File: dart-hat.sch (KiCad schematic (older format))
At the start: 33 parts, among them J0 XT60 Female, J1 Raspberry_Pi_2_3, Q1 Q_PMOS_DSG, Q2 Q_PMOS_DSG, Q3 DMMT5401, U1 CAT24C32YI-GT3

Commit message: power supply overhaul
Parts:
- C1: renamed from C2; footprint Capacitor_SMD:C_0805_2012Metric_Pad1.15x1.40mm_HandSolder -> Capacitor_SMD:C_0603_1608Metric_Pad1.05x0.95mm_HandSolder; Description (none) -> 25V MLCC 10%; Manufacturer_Part_Number (none) -> GRM188R61E106KA73J; PURCHASE-URL (none) -> https://www.mouser.com/ProductDetail/Murata-Electronics/GRM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; category (none) -> EEPROM; package (none) -> 0603
- C2: renamed from C3; footprint Capacitor_SMD:C_0805_2012Metric_Pad1.15x1.40mm_HandSolder -> Capacitor_SMD:C_0603_1608Metric_Pad1.05x0.95mm_HandSolder; Description (none) -> 16V MLCC 10%; Manufacturer_Part_Number (none) -> C0603C104K4RACTU; category (none) -> EEPROM; package (none) -> 0603
- CP1: Description (none) -> 100V Electrolytic 20%; Manufacturer_Part_Number (none) -> 337CKS050M; category (none) -> LIPO; package (none) -> 16mm
- D1: renamed from D2; footprint Diode_SMD:D_SOD-523 -> Diode_SMD:D_SOT-23_ANK; Description (none) -> 15V Zener Diode 5mA 250mW; Manufacturer_Part_Number (none) -> BZX84C15VLYFHT116; category (none) -> LIPO; package (none) -> SOT-23
- D2: renamed from D8; Description (none) -> 1.2V GREEN LED 20mA; Manufacturer_Part_Number (none) -> HSME-C170; category (none) -> GPIO; package (none) -> 0805
- D3: renamed from D9; Description (none) -> 2.1V Amber LED 20mA; Manufacturer_Part_Number (none) -> HSMA-C170; category (none) -> GPIO; package (none) -> 0805
- D4: renamed from D1; footprint Package_TO_SOT_THT:TO-220-2_Horizontal_TabUp -> Diode_SMD:D_SOD-128; Description (none) -> Schottky Diode; Manufacturer_Part_Number (none) -> RB088LAM-40TR; category (none) -> LIPO; package (none) -> SOD-128-2
- F1: footprint Fuse:Fuse_0805_2012Metric_Pad1.15x1.40mm_HandSolder -> Fuse:Fuse_Bourns_MF-SM_7.98x5.44mm; Description (none) -> 6V Fuse 3A Hold 5A Trip; Manufacturer_Part_Number (none) -> MF-LSMF300X-2; category (none) -> SERVO; package (none) -> 3121/MF-SM_7.98x5.44
- J1: renamed from J0; Description (none) -> Female XT60 Receptacle; Manufacturer_Part_Number (none) -> XT60; category (none) -> LIPO; package (none) -> XT60
- J2: renamed from J1; Description (none) -> Raspberry Pi Stackable Header; category (none) -> PI; package (none) -> 2x20x2.54mm
- JP1: Description (none) -> Pin Header; category (none) -> EEPROM; package (none) -> 2x2.54mm
- Q1: footprint Package_TO_SOT_SMD:TO-263-3_TabPin2 -> Package_TO_SOT_SMD:TO-263-2; Description (none) -> 60V 27.5A P-Channel MOSFET (120W Dissipation); Manufacturer_Part_Number (none) -> NTB25P06T4G; category (none) -> LIPO
- Q2: footprint Package_SO:SOIC-8-1EP_3.9x4.9mm_P1.27mm_EP2.29x3mm -> Package_TO_SOT_SMD:TO-263-2; Description (none) -> 60V 27.5A P-Channel MOSFET (120W Dissipation); Manufacturer_Part_Number (none) -> NTB25P06T4G; category (none) -> 5VREG
- Q3: Manufacturer_Part_Number (none) -> DMMT5401; category (none) -> 5VREG
- R1: footprint Resistor_SMD:R_0805_2012Metric_Pad1.15x1.40mm_HandSolder -> Resistor_SMD:R_0603_1608Metric_Pad1.05x0.95mm_HandSolder; Description (none) -> 375mW Resistor 0.1%; Manufacturer_Part_Number (none) -> PHP00603E1002BST1; category (none) -> LIPO; package (none) -> 0603
- R10: renamed from R8; footprint Resistor_SMD:R_0805_2012Metric_Pad1.15x1.40mm_HandSolder -> Resistor_SMD:R_0402_1005Metric; Description (none) -> 63mW Resistor 0.05%; Manufacturer_Part_Number (none) -> ERA-2VRW1001X; category (none) -> EEPROM; package (none) -> 0402
- R11: renamed from R9; Description (none) -> 125mW Resistor 0.1%; Manufacturer_Part_Number (none) -> ERA-6VEB4701V; category (none) -> CAN; package (none) -> 0805
- R12: renamed from R10; Description (none) -> 125mW Resistor 0.1%; Manufacturer_Part_Number (none) -> ERA-6VEB4701V; category (none) -> CAN; package (none) -> 0805
- R13: renamed from R11; Description (none) -> 125mW Resistor 0.1%; Manufacturer_Part_Number (none) -> ERA-6VEB4701V; category (none) -> CAN; package (none) -> 0805
- R2, R3: footprint Resistor_SMD:R_0805_2012Metric_Pad1.15x1.40mm_HandSolder -> Resistor_SMD:R_0603_1608Metric_Pad1.05x0.95mm_HandSolder; Description (none) -> 375mW Resistor 0.1%; Manufacturer_Part_Number (none) -> PHP00603E1002BST1; category (none) -> 5VREG; package (none) -> 0603
- R4: renamed from R23; Description (none) -> 100V 125mW Resistor 0.1%; Manufacturer_Part_Number (none) -> ERA-6VEB1200V; category (none) -> GPIO; package (none) -> 0805
- R5: renamed from R24; value 120 -> 62; footprint Resistor_SMD:R_0805_2012Metric_Pad1.15x1.40mm_HandSolder -> Resistor_SMD:R_1206_3216Metric_Pad1.42x1.75mm_HandSolder; Description (none) -> 100V 250mW Resistor 0.1%; Manufacturer_Part_Number (none) -> ERA-8AED620V; category (none) -> GPIO; package (none) -> 0805
- R6: renamed from R4; footprint Resistor_SMD:R_0805_2012Metric_Pad1.15x1.40mm_HandSolder -> Resistor_SMD:R_0603_1608Metric_Pad1.05x0.95mm_HandSolder; Description (none) -> 100mW Resistor 0.1%; Manufacturer_Part_Number (none) -> ERA-3VEB3901V; category (none) -> EEPROM; package (none) -> 0603
- R7: renamed from R5; footprint Resistor_SMD:R_0805_2012Metric_Pad1.15x1.40mm_HandSolder -> Resistor_SMD:R_0603_1608Metric_Pad1.05x0.95mm_HandSolder; Description (none) -> 100mW Resistor 0.1%; Manufacturer_Part_Number (none) -> ERA-3VEB3901V; category (none) -> EEPROM; package (none) -> 0603
- R8: renamed from R6; Description (none) -> 125mW Resistor 0.1%; Manufacturer_Part_Number (none) -> ERA-6VEB4701V; category (none) -> PI; package (none) -> 0805
- R9: renamed from R7; Description (none) -> 125mW Resistor 0.1%; Manufacturer_Part_Number (none) -> ERA-6VEB4701V; category (none) -> PI; package (none) -> 0805
- U1: Description (none) -> 32kb EEPROM i2c 1mhz; Manufacturer_Part_Number (none) -> CAT24C32YI-GT3; category (none) -> EEPROM; package (none) -> 8-TSSOP
- renumbered TP15 to TP1, TP1 to TP2, TP2 to TP3, TP3 to TP4, TP4 to TP5
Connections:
- net +5V: now also F1.1, TP4.1
- net +5V_SRV: no longer F1.1, TP4.1
- net BEC (pi)/V_OUT renamed 5V Power Supply/VOUT

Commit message: final final sch
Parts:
- removed Q1, Q2: Q_PMOS_DSG, Package_TO_SOT_SMD:TO-263-2, symbol Device:Q_PMOS_DSG
- removed TP3: TestPoint, TestPoint:TestPoint_Pad_D1.0mm, symbol Connector:TestPoint
- added Q1, Q2: SI7611DN-T1-GE3, SI7611DN-T1-GE3:VISHAY_SIS468DN-T1-GE3, symbol SI7611DN-T1-GE3:SI7611DN-T1-GE3
- CP1: value 330uF -> 470uF; footprint Capacitor_THT:CP_Radial_D10.0mm_P5.00mm -> Capacitor_SMD:CP_Elec_10x10.5; Description 100V Electrolytic 20% -> 6.3V SMD Electrolytic 20%; Manufacturer_Part_Number 337CKS050M -> APXH6R3ARA471MJ80G; category LIPO -> 5VREG; package 16mm -> (none)
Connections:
- net +5V: now also Q2.1, Q2.2, Q2.3
- net +BATT: now also Q1.1, Q1.2, Q1.3
- net 5V Power Supply/VOUT: now also Q2.5, Q2.6, Q2.7, Q2.8, Q2.9
- net at J1.1 (Pin_1): now also Q1.5, Q1.6, Q1.7, Q1.8, Q1.9
- net at D1.2 (A), R1.1, TP2.1: now also Q1.4
- net at Q3.4, R3.1: now also Q2.4
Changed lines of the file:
@@
-$EndComp
-$Comp
-L Device:Q_PMOS_DSG Q?
-U 1 1 619F5A9A
-P 1700 1150
-AR Path="/61AC98FF/619F5A9A" Ref="Q?"  Part="1"
-AR Path="/619F5A9A" Ref="Q1"  Part="1"
-F 0 "Q1" V 2042 1150 50  0000 C CNN
-F 1 "Q_PMOS_DSG" V 1951 1150 50  0000 C CNN
-F 2 "Package_TO_SOT_SMD:TO-263-2" H 1900 1250 50  0001 C CNN
-F 3 "~" H 1700 1150 50  0001 C CNN
-F 4 "60V 27.5A P-Channel MOSFET (120W Dissipation)" H 1700 1150 50  0001 C CNN "Description"
-F 5 "NTB25P06T4G" H 1700 1150 50  0001 C CNN "Manufacturer_Part_Number"
-F 6 "LIPO" H 1700 1150 50  0001 C CNN "category"
-	1    1700 1150
-	0    -1   -1   0
-$EndComp
-$Comp
-L Device:CP_Small CP?
-U 1 1 619F5AAC
-P 2750 1250
-AR Path="/61AC98FF/619F5AAC" Ref="CP?"  Part="1"
-AR Path="/619F5AAC" Ref="CP1"  Part="1"
-F 0 "CP1" H 2838 1296 50  0000 L CNN
-F 1 "330uF" H 2838 1205 50  0000 L CNN
-F 2 "Capacitor_THT:CP_Radial_D10.0mm_P5.00mm" H 2750 1250 50  0001 C CNN
-F 3 "~" H 2750 1250 50  0001 C CNN
-F 4 "100V Electrolytic 20%" H 2750 1250 50  0001 C CNN "Description"
-F 5 "337CKS050M" H 2750 1250 50  0001 C CNN "Manufacturer_Part_Number"
-F 6 "LIPO" H 2750 1250 50  0001 C CNN "category"
-F 7 "16mm" H 2750 1250 50  0001 C CNN "package"
-	1    2750 1250
-	1    0    0    -1
 $EndComp
 $Comp
@@
 	1700 1500 1700 1350
 Wire Wire Line
-	1700 1350 2100 1350
-Connection ~ 1700 1350
+	1700 1350 1800 1350
 Connection ~ 2750 1050
 Wire Wire Line
@@
 	2400 3800 2550 3800
 Wire Wire Line
-	2550 3100 2100 3100
+	2550 3100 2200 3100
 Connection ~ 2400 3800
 Wire Wire Line
@@
 Wire Wire Line
 	2100 900  2100 1050
-$Comp
-L Connector:TestPoint TP3
-U 1 1 61B7B3D6
-P 2650 2800
-F 0 "TP3" H 2592 2872 50  0000 R CNN
-F 1 "TestPoint" H 2592 2917 50  0001 R CNN
-F 2 "TestPoint:TestPoint_Pad_D1.0mm" H 2850 2800 50  0001 C CNN
-F 3 "~" H 2850 2800 50  0001 C CNN
-	1    2650 2800
-	-1   0    0    1
-$EndComp
-Connection ~ 2650 2800
 Wire Wire Line
 	8800 4900 8900 4900
@@
 	1    0    0    -1
 $EndComp
-$Comp
-L Device:Q_PMOS_DSG Q?
-U 1 1 61A72D78
-P 2100 2900
-AR Path="/61AC98FF/61A72D78" Ref="Q?"  Part="1"
-AR Path="/61A72D78" Ref="Q2"  Part="1"
-F 0 "Q2" V 2442 2900 50  0000 C CNN
-F 1 "Q_PMOS_DSG" V 2351 2900 50  0000 C CNN
-F 2 "Package_TO_SOT_SMD:TO-263-2" H 2300 3000 50  0001 C CNN
-F 3 "~" H 2100 2900 50  0001 C CNN
-F 4 "5VREG" H 2100 2900 50  0001 C CNN "category"
-F 5 "60V 27.5A P-Channel MOSFET (120W Dissipation)" H 2100 2900 50  0001 C CNN "Description"
-F 6 "NTB25P06T4G" H 2100 2900 50  0001 C CNN "Manufacturer_Part_Number"
-	1    2100 2900
-	0    -1   -1   0
-$EndComp
 $Sheet
 S 1300 5200 600  550
@@
 	1    0    0    -1
 $EndComp
+$Comp
+L Device:CP_Small CP?
+U 1 1 61B8B78F
+P 2750 1250
+AR Path="/61BC5F5B/61B8B78F" Ref="CP?"  Part="1"
+AR Path="/61B8B78F" Ref="CP1"  Part="1"
+F 0 "CP1" H 2838 1296 50  0000 L CNN
+F 1 "470uF" H 2838 1205 50  0000 L CNN
+F 2 "Capacitor_SMD:CP_Elec_10x10.5" H 2750 1250 50  0001 C CNN
+F 3 "~" H 2750 1250 50  0001 C CNN
+F 4 "6.3V SMD Electrolytic 20%" H 2750 1250 50  0001 C CNN "Description"
+F 5 "APXH6R3ARA471MJ80G" H 2750 1250 50  0001 C CNN "Manufacturer_Part_Number"
+F 6 "5VREG" H 2750 1250 50  0001 C CNN "category"
+	1    2750 1250
+	1    0    0    -1
+$EndComp
+$Comp
+L SI7611DN-T1-GE3:SI7611DN-T1-GE3 Q1
+U 1 1 61BC9EE3
+P 1700 1150
+F 0 "Q1" V 2045 1150 50  0000 C CNN
+F 1 "SI7611DN-T1-GE3" V 1954 1150 50  0000 C CNN
+F 2 "SI7611DN-T1-GE3:VISHAY_SIS468DN-T1-GE3" H 1700 1150 50  0001 L BNN
+F 3 "" H 1700 1150 50  0001 L BNN
+F 4 "VISHAY" H 1700 1150 50  0001 L BNN "MANUFACTURER"
+F 5 "B" H 1700 1150 50  0001 L BNN "PARTREV"
+F 6 "Manufacturer recommendations" H 1700 1150 50  0001 L BNN "STANDARD"
+	1    1700 1150
+	0    1    -1   0
+$EndComp
+Wire Wire Line
+	1800 1250 1800 1350
+Connection ~ 1800 1350
+Wire Wire Line
+	1800 1350 2100 1350
+$Comp
+L SI7611DN-T1-GE3:SI7611DN-T1-GE3 Q2
+U 1 1 61BE0D47
+P 2100 2900
+F 0 "Q2" V 2445 2900 50  0000 C CNN
+F 1 "SI7611DN-T1-GE3" V 2354 2900 50  0000 C CNN
+F 2 "SI7611DN-T1-GE3:VISHAY_SIS468DN-T1-GE3" H 2100 2900 50  0001 L BNN
+F 3 "" H 2100 2900 50  0001 L BNN
+F 4 "VISHAY" H 2100 2900 50  0001 L BNN "MANUFACTURER"
+F 5 "B" H 2100 2900 50  0001 L BNN "PARTREV"
+F 6 "Manufacturer recommendations" H 2100 2900 50  0001 L BNN "STANDARD"
+	1    2100 2900
+	0    1    -1   0
+$EndComp
+Wire Wire Line
+	2200 3000 2200 3100
 $EndSCHEMATC

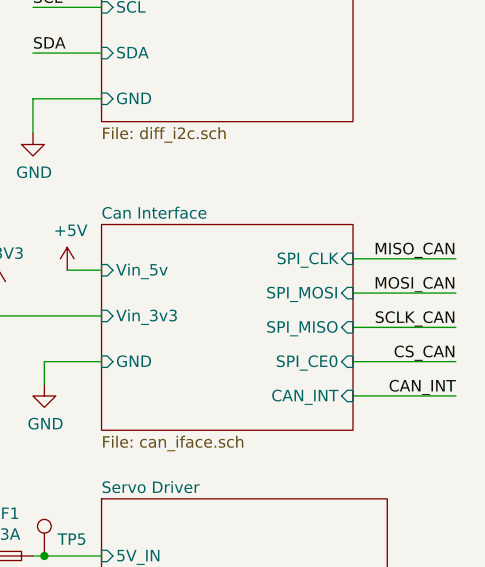
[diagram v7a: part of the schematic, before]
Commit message: [rev.2 fixes]  - fix Q4 net pin assignment  - removed UVLO  - fix kelvin connection on R_sense  - fix MCP2515 symbol + pinout  - changed oscillator capacitors for 18uF load capacitance  - PCA9615 biasing resistors
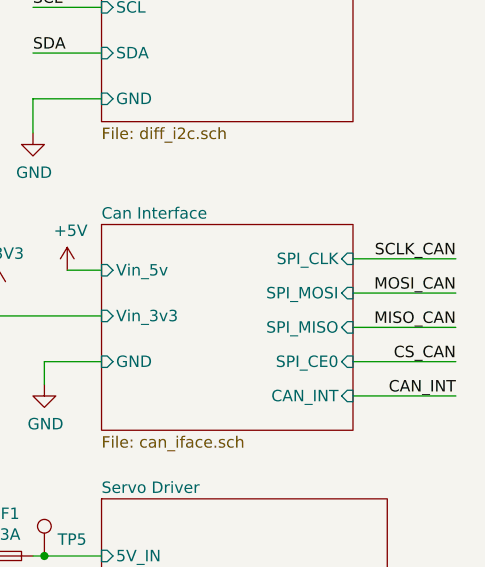
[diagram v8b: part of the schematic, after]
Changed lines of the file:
@@
 Text Label 11100 3750 2    50   ~ 0
 MOSI_CAN
-Text Label 11100 3900 2    50   ~ 0
+Text Label 11100 3600 2    50   ~ 0
 SCLK_CAN
-Wire Wire Line
-	9100 3850 9100 3750
 Wire Wire Line
 	9550 4050 9300 4050
@@
 Wire Wire Line
 	5850 3800 6350 3800
-Text Label 11100 3600 2    50   ~ 0
+Text Label 11100 3900 2    50   ~ 0
 MISO_CAN
 Wire Wire Line
+	10650 3900 11100 3900
+Wire Wire Line
+	10650 3750 11100 3750
+Wire Wire Line
 	10650 3600 11100 3600
-Wire Wire Line
-	10650 3750 11100 3750
-Wire Wire Line
-	10650 3900 11100 3900
 Wire Wire Line
 	10650 4050 11100 4050
@@
 CAN_INT
 $Comp
-L power:+3V3 #PWR023
-U 1 1 61CB860A
-P 9100 3750
-F 0 "#PWR023" H 9100 3600 50  0001 C CNN
-F 1 "+3V3" H 9115 3923 50  0000 C CNN
-F 2 "" H 9100 3750 50  0001 C CNN
-F 3 "" H 9100 3750 50  0001 C CNN
-	1    9100 3750
-	1    0    0    -1
-$EndComp
-$Comp
 L power:+3V3 #PWR027
 U 1 1 61CE4F5D
@@
 Wire Wire Line
 	2200 3000 2200 3100
+Wire Wire Line
+	9100 3850 9100 3750
+$Comp
+L power:+3V3 #PWR023
+U 1 1 61CB860A
+P 9100 3750
+F 0 "#PWR023" H 9100 3600 50  0001 C CNN
+F 1 "+3V3" H 9115 3923 50  0000 C CNN
+F 2 "" H 9100 3750 50  0001 C CNN
+F 3 "" H 9100 3750 50  0001 C CNN
+	1    9100 3750
+	1    0    0    -1
+$EndComp
 $EndSCHEMATC
